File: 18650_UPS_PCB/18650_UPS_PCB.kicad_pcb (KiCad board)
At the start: 4 copper layers, 90 x 22 mm, 59 parts, among them J1 USB_B_Micro, J2 Conn_02x04_Odd_Even, SW1 SW_SPDT, SW2 ALPSALPINE_SKRHADE011, U1 STLINK-V3MINI, U2 R5478, U3 STC4054, U4 FS8205A, U5 TPS63000, U6 TPS63000, U7 INA219AxD, U8 SSD1306_128_32, U9 STM32F030F4Px

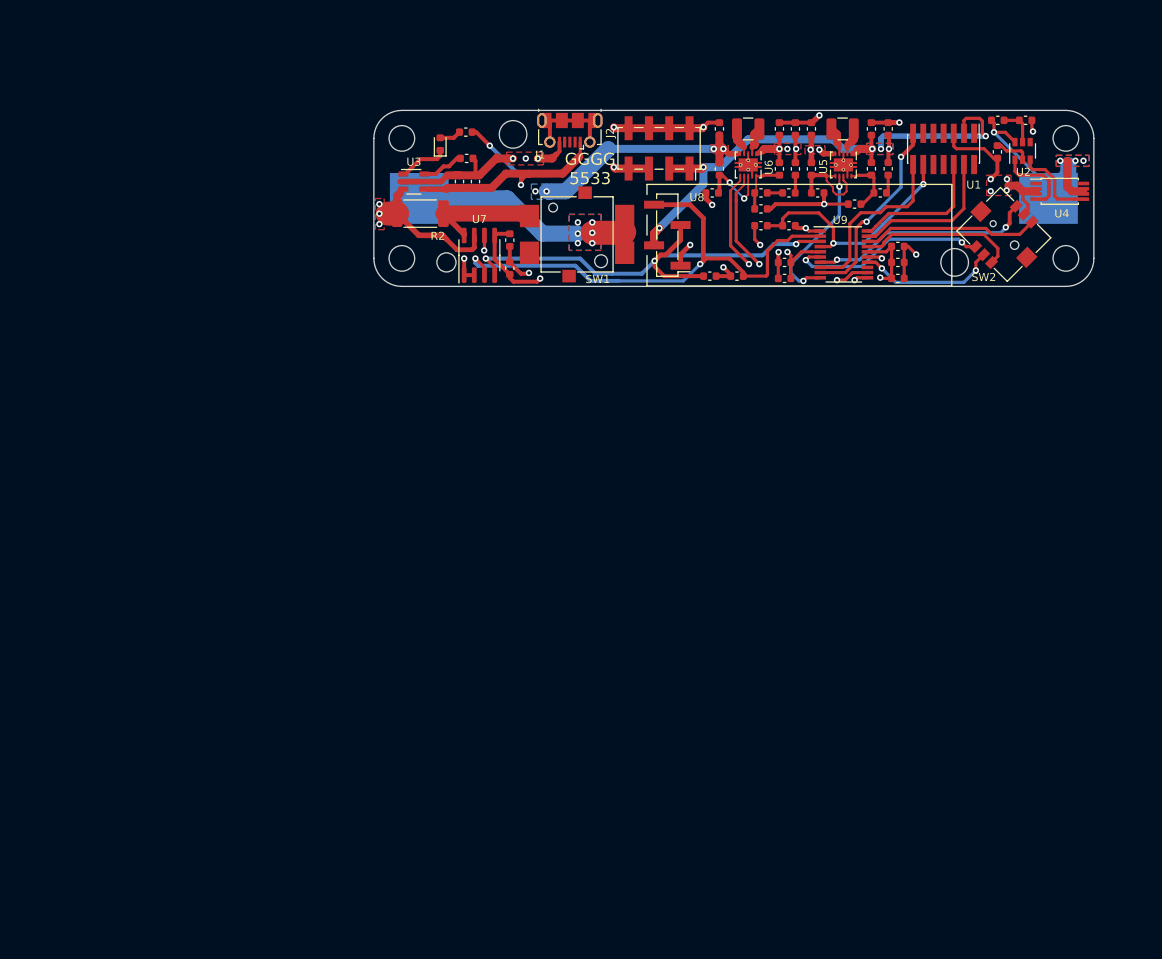
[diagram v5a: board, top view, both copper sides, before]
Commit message: v2 layout started
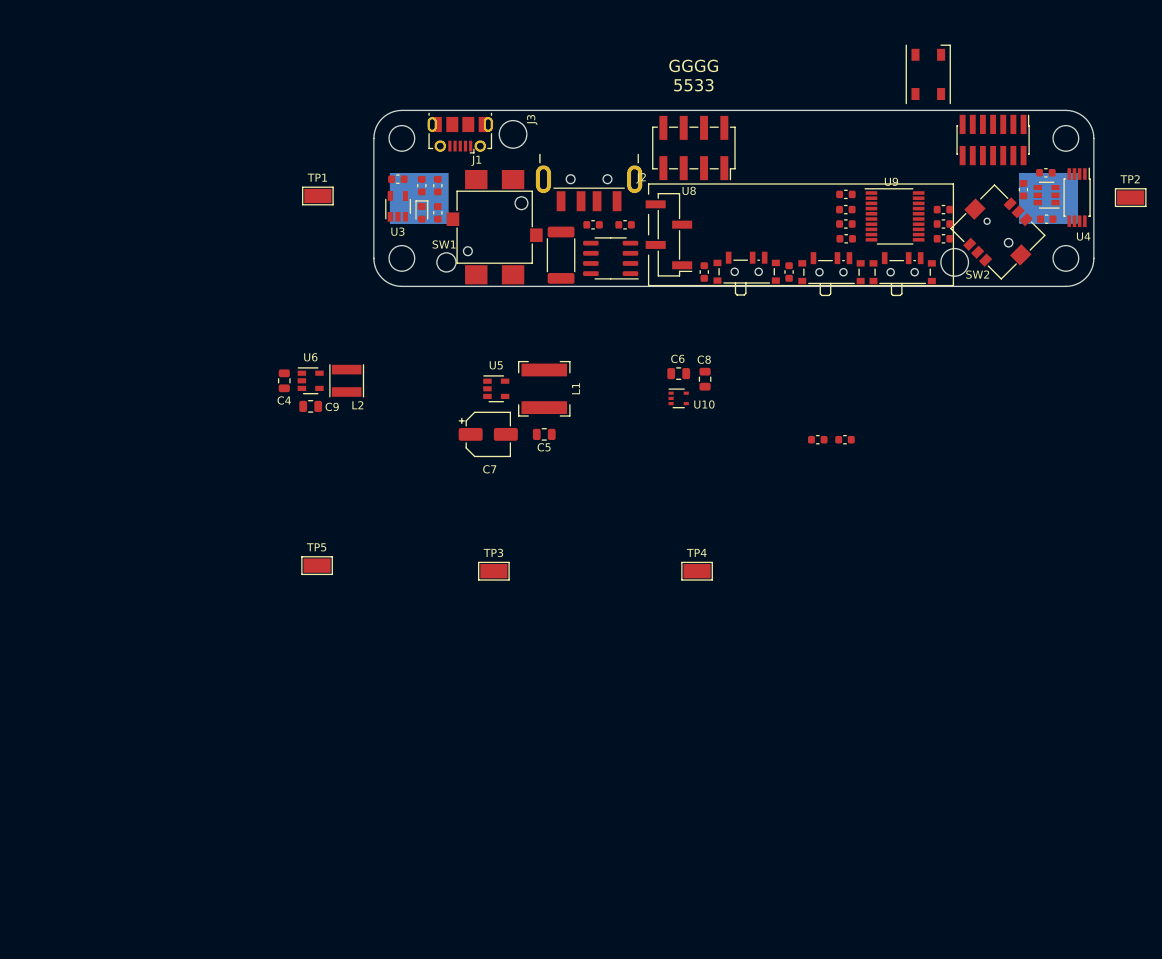
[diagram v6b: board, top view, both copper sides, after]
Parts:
- removed C10, C20, C21: 10 uF, Capacitor_SMD:C_0603_1608Metric
- removed C11: 1.2 pF, Capacitor_SMD:C_0603_1608Metric
- removed R10, R11: 1 MOhm, Resistor_SMD:R_0603_1608Metric
- removed R14: 680 kOhm, Resistor_SMD:R_0603_1608Metric
- removed R15: 100 kOhm, Resistor_SMD:R_0603_1608Metric
- removed R16: 120 kOhm, Resistor_SMD:R_0603_1608Metric
- removed R8, R9: 200 kOhm, Resistor_SMD:R_0603_1608Metric
- added D2: WS2812B, LED_SMD:LED_WS2812B_PLCC4_5.0x5.0mm_P3.2mm, F.Cu at (190.1, 69.7)
- added J3: USB_A, Connector_USB:USB_A_CNCTech_1001-011-01101_Horizontal, F.Cu at (147.7, 75.9)
- added SW3: SW_SPDT, Button_Switch_SMD:SW_SPDT_PCM12, F.Cu at (167.4, 94.0)
- added SW4: SW_SPDT, Button_Switch_SMD:SW_SPDT_PCM12, F.Cu at (178.0, 94.1)
- added SW5: SW_SPDT, Button_Switch_SMD:SW_SPDT_PCM12, F.Cu at (186.9, 94.1)
- added TP1: TestPoint, TestPoint:TestPoint_Keystone_5015_Micro-Minature, F.Cu at (113.8, 84.9)
- added TP2: TestPoint, TestPoint:TestPoint_Keystone_5015_Micro-Minature, F.Cu at (215.4, 85.1)
- added TP3: TestPoint, TestPoint:TestPoint_Keystone_5015_Micro-Minature, F.Cu at (135.8, 131.8)
- added TP4: TestPoint, TestPoint:TestPoint_Keystone_5015_Micro-Minature, F.Cu at (161.2, 131.8)
- added TP5: TestPoint, TestPoint:TestPoint_Keystone_5015_Micro-Minature, F.Cu at (113.7, 131.1)
- added U10: LR9102G-xx, Package_TO_SOT_SMD:SOT-353_SC-70-5, F.Cu at (158.9, 110.2)
- C13, C14: value 0.1 uF -> 100 nF
- C2: value 0.01 uF -> 10 nF
- C4: value 10uF -> 4.7 uF; footprint Capacitor_SMD:C_0603_1608Metric -> Capacitor_SMD:C_0805_2012Metric
- C5: value 10uF -> 10 uF; footprint Capacitor_SMD:C_0603_1608Metric -> Capacitor_SMD:C_0805_2012Metric
- C6: value 0.1uF -> 1 uF; footprint Capacitor_SMD:C_0603_1608Metric -> Capacitor_SMD:C_0805_2012Metric
- C7: value 0.1uF -> 100 uF; footprint Capacitor_SMD:C_0603_1608Metric -> Capacitor_SMD:CP_Elec_5x5.4
- C8: value 10 uF -> 1 uF; footprint Capacitor_SMD:C_0603_1608Metric -> Capacitor_SMD:C_0805_2012Metric
- C9: value 2.2 pF -> 10 uF; footprint Capacitor_SMD:C_0603_1608Metric -> Capacitor_SMD:C_0805_2012Metric
- L1: value 2.2uH -> 22 uH; footprint Inductor_SMD:L_1210_3225Metric -> Inductor_SMD:L_Bourns-SRN6028
- L2: value 2.2uH -> 1.5 uH; footprint Inductor_SMD:L_1210_3225Metric -> Inductor_SMD:L_Taiyo-Yuden_MD-4040
- R6, R7: value 100 Ohm -> 10 kOhm
- U5: value TPS63000 -> ME2188Cxx; footprint Package_SON:Texas_DRC0010J_ThermalVias -> Package_TO_SOT_SMD:SOT-23-5
- U6: value TPS63000 -> XC9236Axx; footprint Package_SON:Texas_DRC0010J_ThermalVias -> Package_TO_SOT_SMD:SOT-23-5
- moved C9 76.1 mm to (112.9, 111.2), turned to 180 degrees
- moved C4 73.0 mm to (109.6, 108.0)
- moved U6 61.0 mm to (112.9, 108.0), turned to 0 degrees
- moved L2 59.2 mm to (117.4, 108.0), turned to 270 degrees
- moved U5 51.6 mm to (136.1, 109.0), turned to 0 degrees
- moved L1 49.5 mm to (142.1, 109.0), turned to 90 degrees
- moved C5 44.0 mm to (142.1, 114.7), turned to 180 degrees
- moved C7 41.2 mm to (135.1, 114.7)
- moved C8 38.8 mm to (162.2, 107.8)
- moved C6 28.5 mm to (158.9, 107.1), turned to 0 degrees
- moved R12 24.5 mm to (179.7, 115.3)
- moved R13 24.5 mm to (176.3, 115.3)
- moved R6 18.6 mm to (162.1, 94.4)
- moved R2 18.4 mm to (144.2, 92.3), turned to 270 degrees
- moved U7 16.4 mm to (150.4, 92.7), turned to 180 degrees
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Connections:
- C12 pad 1: +3V3 -> +3.3VA
- C13 pad 1: +3V3 -> +3.3VA
- C15 pad 2: +3V3 -> +3.3VA
- C16 pad 2: +3V3 -> +3.3VA
- C17 pad 2: +3V3 -> +3.3VA
- C18 pad 1: +3V3 -> +3.3VA
- C19 pad 1: +3V3 -> +3.3VA
- C4 pad 1: GNDD -> Shunt-
- C4 pad 2: Shunt- -> GNDD
- C5 pad 1: GNDD -> Shunt-
- C5 pad 2: Shunt- -> GNDD
- C6 pad 1: GNDD -> Shunt-
- C6 pad 2: Net-(C6-Pad2) -> GNDD
- C7 pad 1: GNDD -> +5V
- C7 pad 2: Net-(C7-Pad2) -> GNDD
- C8 pad 1: +3V3 -> +3.3VA
- C9 pad 2: Net-(C9-Pad2) -> GNDD
- L1 pad 1: Net-(L1-Pad1) -> Shunt-
- L2 pad 2: Net-(L2-Pad2) -> +3V3
- R17 pad 1: +3V3 -> +3.3VA
- R6 pad 1: Shunt- -> PA0
- R6 pad 2: Net-(C6-Pad2) -> GNDD
- R7 pad 1: Shunt- -> PA1
- R7 pad 2: Net-(C7-Pad2) -> GNDD
- SW2 pad 1: PA0 -> PA4
- SW2 pad 2: PB1 -> PA10
- SW2 pad 3: PA9 -> PA6
- SW2 pad 4: PA1 -> PA5
- SW2 pad 6: PA10 -> PA9
- U1 pad 3: +3V3 -> +3.3VA
- U4 pad 4: Net-(U2-Pad1) -> Net-(U2-Pad3)
- U4 pad 5: Net-(U2-Pad3) -> Net-(U2-Pad1)
- U5 pad 1: +3V3 -> BoostCE
- U5 pad 2: Net-(L1-Pad2) -> +5V
- U5 pad 3: GNDD -> Net-(U5-Pad3)
- U5 pad 4: Net-(L1-Pad1) -> GNDD
- U5 pad 5: Shunt- -> Net-(L1-Pad2)
- U6 pad 1: +5V -> Shunt-
- U6 pad 2: Net-(L2-Pad2) -> GNDD
- U6 pad 3: GNDD -> BuckCE
- U6 pad 4: Net-(L2-Pad1) -> +3V3
- U6 pad 5: Shunt- -> Net-(L2-Pad1)
- U7 pad 5: +3V3 -> +3.3VA
- U8 pad 2: +3V3 -> +3.3VA
- U9 pad 13: Net-(U9-Pad13) -> PA7
- U9 pad 16: +3V3 -> +3.3VA
- U9 pad 5: +3V3 -> +3.3VA
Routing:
- net +3V3: track 157.4 -> 0.00 mm, vias 11 -> 0
- net -BATT: track 125.6 -> 0.00 mm, vias 7 -> 0
- net Shunt-: track 117.5 -> 0.00 mm, vias 10 -> 0
- net GNDD: track 87.1 -> 0.00 mm, vias 18 -> 0
- net I2C1_SDA: track 66.1 -> 0.00 mm, vias 2 -> 0
- net I2C1_SCL: track 60.3 -> 0.00 mm, vias 3 -> 0
- net +5V: track 37.4 -> 0.00 mm, vias 4 -> 0
- net VCC: track 33.9 -> 0.00 mm, vias 2 -> 0
- net NRST: track 30.8 -> 0.00 mm, vias 2 -> 0
- net Net-(BT1-Pad1): track 30.3 -> 0.00 mm, vias 6 -> 0
- net PA6: track 28.5 -> 0.00 mm, vias 2 -> 0
- net PA1: track 28.3 -> 0.00 mm, vias 2 -> 0
- net PA5: track 27.1 -> 0.00 mm, vias 2 -> 0
- net PA0: track 25.3 -> 0.00 mm, vias 2 -> 0
- net USART1_RX: track 24.3 -> 0.00 mm, vias 2 -> 0
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- removed copper zone on B.Cu, net +3V3
- removed copper zone on F.Cu, net +3V3
- removed copper zone on In2.Cu, net +3V3
- removed copper zone on F.Cu, net +5V
- removed copper zone on In2.Cu, net +5V
- removed copper zone on B.Cu, net -BATT
- removed copper zone on F.Cu, net -BATT
- removed copper zone on In2.Cu, net -BATT
- removed copper zone on F.Cu, net GNDD
- removed copper zone on In1.Cu, net GNDD
- removed copper zone on B.Cu, net Net-(BT1-Pad1)
- removed copper zone on F.Cu, net Net-(BT1-Pad1)
- removed copper zone on B.Cu, net Shunt-
- removed copper zone on F.Cu, net Shunt-
- removed copper zone on In2.Cu, net Shunt-

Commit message: all components on board
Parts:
- removed TP1, TP2, TP3, TP4, TP5: TestPoint, TestPoint:TestPoint_Keystone_5015_Micro-Minature
- moved C4 70.1 mm to (176.8, 88.0), turned to 90 degrees
- moved C9 66.1 mm to (173.5, 84.8), turned to 0 degrees
- moved U6 63.8 mm to (173.5, 88.0), turned to 180 degrees
- moved C7 59.8 mm to (183.0, 78.9), turned to 90 degrees
- moved L2 55.3 mm to (169.0, 88.0), turned to 90 degrees
- moved C5 52.0 mm to (177.4, 76.5), turned to 0 degrees
- moved U5 50.5 mm to (177.5, 80.1), turned to 180 degrees
- moved L1 42.1 mm to (171.5, 78.9), turned to 270 degrees
- moved R12 36.3 mm to (155.2, 88.6), turned to 90 degrees
- moved R13 29.1 mm to (160.4, 91.0), turned to 90 degrees
- moved U10 24.7 mm to (161.6, 85.6), turned to 270 degrees
- moved C6 22.3 mm to (164.7, 85.6), turned to 270 degrees
- moved C8 19.0 mm to (164.0, 88.9), turned to 0 degrees
- moved D2 9.11 mm to (189.6, 78.8)
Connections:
- R12 pad 1: +3V3 -> +3.3VA
- R13 pad 1: +3V3 -> +3.3VA

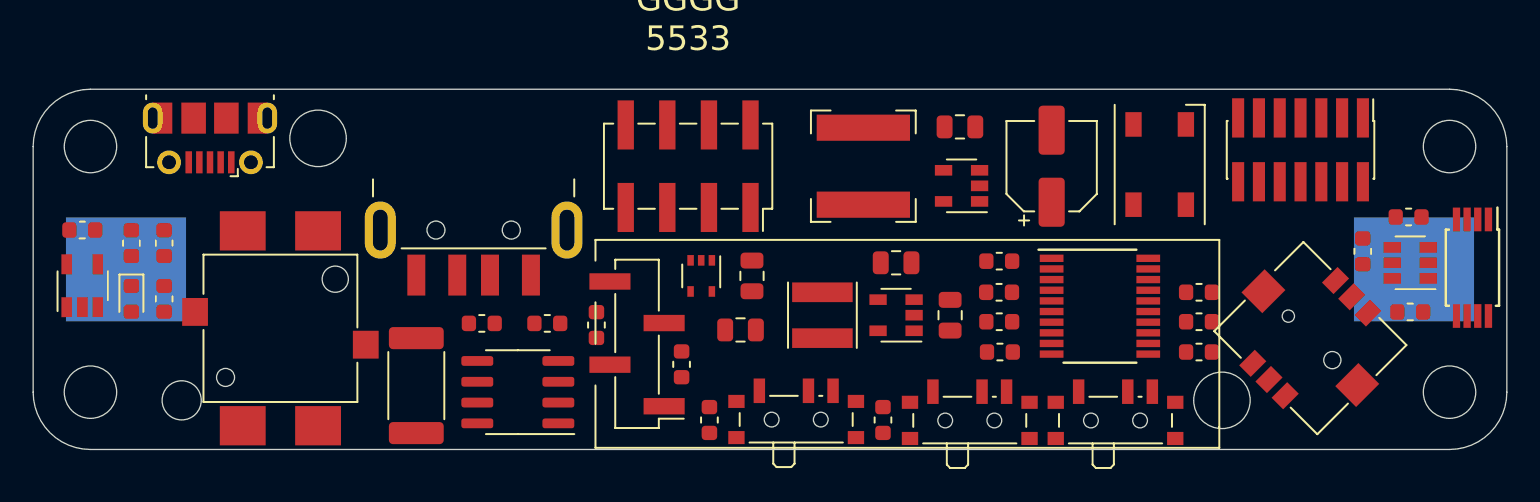
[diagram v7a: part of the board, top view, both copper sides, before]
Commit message: v2 layout complete and started routing
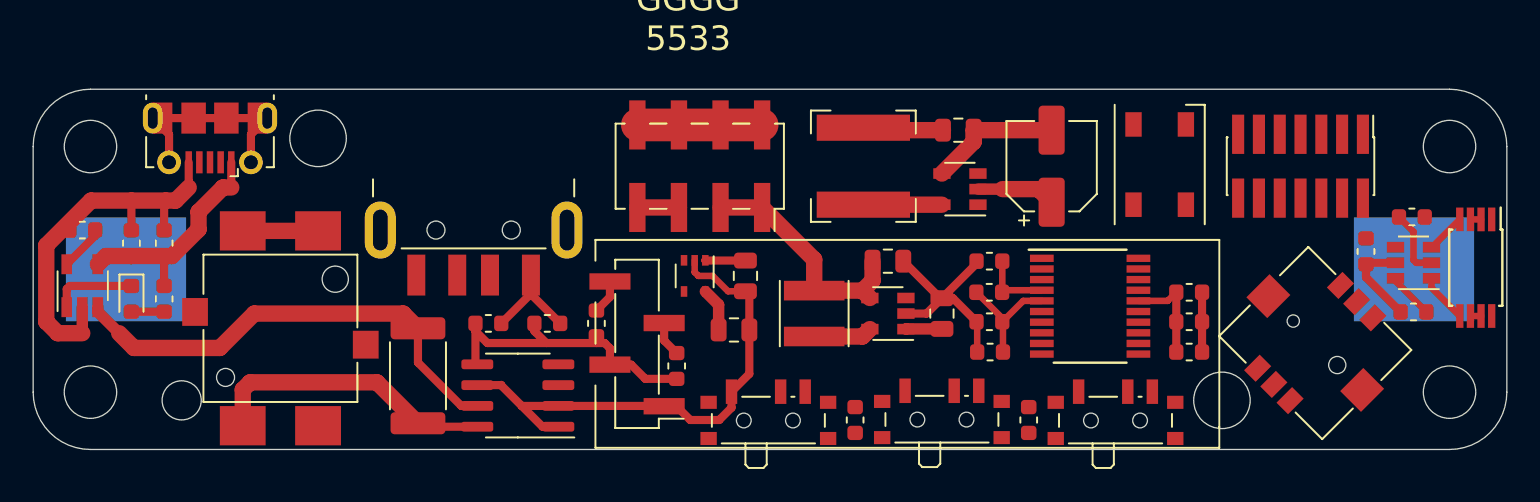
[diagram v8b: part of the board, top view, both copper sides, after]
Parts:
- moved SW5 21.2 mm to (165.7, 94.1)
- moved R7 8.90 mm to (181.6, 94.4)
- moved SW3 8.90 mm to (176.3, 94.0)
- moved SW4 8.90 mm to (186.9, 94.1)
- moved R6 8.90 mm to (171.0, 94.4)
- moved R13 5.77 mm to (155.2, 88.5)
- moved R12 5.50 mm to (160.1, 91.1)
- moved U1 1.00 mm to (198.2, 78.9)
- moved J2 0.71 mm to (161.5, 78.9)
- moved R2 0.61 mm to (144.3, 91.7)
- moved R17 0.60 mm to (179.2, 86.6)
- moved C14 0.60 mm to (179.2, 84.7)
- moved C15 0.60 mm to (191.4, 90.2)
- moved C16 0.60 mm to (191.4, 88.4)
- moved C17 0.60 mm to (191.4, 86.6)
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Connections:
- R12 pad 2: I2C1_SDA -> I2C1_SCL
- R13 pad 2: I2C1_SCL -> I2C1_SDA
- SW2 pad 2: PA10 -> PF1
- SW2 pad 6: PA9 -> PF0
- U9 pad 17: PA9 -> I2C1_SCL
- U9 pad 18: PA10 -> I2C1_SDA
- U9 pad 2: I2C1_SDA -> PF0
- U9 pad 3: I2C1_SCL -> PF1
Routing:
- net GNDD: track 0.00 -> 72.6 mm
- net Shunt-: track 0.00 -> 38.4 mm
- net +3.3VA: track 0.00 -> 35.4 mm
- net -BATT: track 0.00 -> 27.6 mm
- net Shunt+: track 0.00 -> 17.8 mm
- net +3V3: track 0.00 -> 14.6 mm
- net VCC: track 0.00 -> 14.1 mm
- net Net-(J1-Pad6): track 0.00 -> 12.6 mm
- net +5V: track 0.00 -> 7.37 mm
- net Net-(C2-Pad2): track 0.00 -> 5.62 mm
- net Net-(D1-Pad1): track 0.00 -> 5.14 mm
- net Net-(L1-Pad2): track 0.00 -> 4.80 mm
- net Net-(BT1-Pad1): track 0.00 -> 4.60 mm
- net NRST: track 0.00 -> 4.38 mm
- net Net-(R4-Pad2): track 0.00 -> 4.17 mm
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- added copper zone on In1.Cu, net GNDD
